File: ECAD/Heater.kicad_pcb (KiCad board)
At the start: 2 copper layers, 200 x 200 mm, 11 parts, among them J1 Conn_01x01_Female, J2 Conn_01x01_Female

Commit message: Cleanup
Renamed files, removed temp files
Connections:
- net /+ renamed Net-(J1-Pad1)
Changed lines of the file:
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@@
-(kicad_pcb (version 20171130) (host pcbnew "(5.1.9)-1")
+(kicad_pcb (version 20171130) (host pcbnew "(5.1.10)-1")
   (general
     (thickness 1.6)
@@
   )
   (net 0 "")
-  (net 1 /+)
+  (net 1 "Net-(J1-Pad1)")
   (net_class Default "This is the default net class."
     (clearance 0.2)
@@
     (uvia_dia 0.3)
     (uvia_drill 0.1)
-    (add_net /+)
+    (add_net "Net-(J1-Pad1)")
   )
   (module MountingHole:MountingHole_3.2mm_M3 (layer F.Cu)
@@
       (effects (font (size 1 1) (thickness 0.15)))
     )
-    (fp_circle (center 0 0) (end 3.45 0) (layer F.CrtYd) (width 0.05))
-    (fp_circle (center 0 0) (end 3.2 0) (layer Cmts.User) (width 0.15))
+    (fp_circle (center 0 0) (end 3.2 0) (layer Cmts.User) (width 0.15))
+    (fp_circle (center 0 0) (end 3.45 0) (layer F.CrtYd) (width 0.05))
     (fp_text user %R (at 0.3 0) (layer F.Fab)
       (effects (font (size 1 1) (thickness 0.15)))
@@
       (effects (font (size 1 1) (thickness 0.15)))
     )
-    (fp_circle (center 0 0) (end 3.45 0) (layer F.CrtYd) (width 0.05))
-    (fp_circle (center 0 0) (end 3.2 0) (layer Cmts.User) (width 0.15))
+    (fp_circle (center 0 0) (end 3.2 0) (layer Cmts.User) (width 0.15))
+    (fp_circle (center 0 0) (end 3.45 0) (layer F.CrtYd) (width 0.05))
     (fp_text user %R (at 0.3 0) (layer F.Fab)
       (effects (font (size 1 1) (thickness 0.15)))
@@
       (effects (font (size 1 1) (thickness 0.15)))
     )
-    (fp_circle (center 0 0) (end 3.45 0) (layer F.CrtYd) (width 0.05))
-    (fp_circle (center 0 0) (end 3.2 0) (layer Cmts.User) (width 0.15))
+    (fp_circle (center 0 0) (end 3.2 0) (layer Cmts.User) (width 0.15))
+    (fp_circle (center 0 0) (end 3.45 0) (layer F.CrtYd) (width 0.05))
     (fp_text user %R (at 0.3 0) (layer F.Fab)
       (effects (font (size 1 1) (thickness 0.15)))
@@
       (effects (font (size 1 1) (thickness 0.15)))
     )
-    (fp_circle (center 0 0) (end 3.45 0) (layer F.CrtYd) (width 0.05))
-    (fp_circle (center 0 0) (end 3.2 0) (layer Cmts.User) (width 0.15))
+    (fp_circle (center 0 0) (end 3.2 0) (layer Cmts.User) (width 0.15))
+    (fp_circle (center 0 0) (end 3.45 0) (layer F.CrtYd) (width 0.05))
     (fp_text user %R (at 0.3 0) (layer F.Fab)
       (effects (font (size 1 1) (thickness 0.15)))
@@
       (effects (font (size 1 1) (thickness 0.15)))
     )
-    (fp_circle (center 0 0) (end 3.45 0) (layer F.CrtYd) (width 0.05))
-    (fp_circle (center 0 0) (end 3.2 0) (layer Cmts.User) (width 0.15))
+    (fp_circle (center 0 0) (end 3.2 0) (layer Cmts.User) (width 0.15))
+    (fp_circle (center 0 0) (end 3.45 0) (layer F.CrtYd) (width 0.05))
     (fp_text user %R (at 0.3 0) (layer F.Fab)
       (effects (font (size 1 1) (thickness 0.15)))
@@
       (effects (font (size 1 1) (thickness 0.15)))
     )
-    (fp_circle (center 0 0) (end 3.45 0) (layer F.CrtYd) (width 0.05))
-    (fp_circle (center 0 0) (end 3.2 0) (layer Cmts.User) (width 0.15))
+    (fp_circle (center 0 0) (end 3.2 0) (layer Cmts.User) (width 0.15))
+    (fp_circle (center 0 0) (end 3.45 0) (layer F.CrtYd) (width 0.05))
     (fp_text user %R (at 0.3 0) (layer F.Fab)
       (effects (font (size 1 1) (thickness 0.15)))
@@
       (effects (font (size 1 1) (thickness 0.15)))
     )
-    (fp_circle (center 0 0) (end 3.45 0) (layer F.CrtYd) (width 0.05))
-    (fp_circle (center 0 0) (end 3.2 0) (layer Cmts.User) (width 0.15))
+    (fp_circle (center 0 0) (end 3.2 0) (layer Cmts.User) (width 0.15))
+    (fp_circle (center 0 0) (end 3.45 0) (layer F.CrtYd) (width 0.05))
     (fp_text user %R (at 0.3 0) (layer F.Fab)
       (effects (font (size 1 1) (thickness 0.15)))
@@
       (effects (font (size 1 1) (thickness 0.15)))
     )
-    (fp_circle (center 0 0) (end 3.45 0) (layer F.CrtYd) (width 0.05))
-    (fp_circle (center 0 0) (end 3.2 0) (layer Cmts.User) (width 0.15))
+    (fp_circle (center 0 0) (end 3.2 0) (layer Cmts.User) (width 0.15))
+    (fp_circle (center 0 0) (end 3.45 0) (layer F.CrtYd) (width 0.05))
     (fp_text user %R (at 0.3 0) (layer F.Fab)
       (effects (font (size 1 1) (thickness 0.15)))
@@
       (effects (font (size 1 1) (thickness 0.15)))
     )
-    (fp_circle (center 0 0) (end 3.45 0) (layer F.CrtYd) (width 0.05))
-    (fp_circle (center 0 0) (end 3.2 0) (layer Cmts.User) (width 0.15))
+    (fp_circle (center 0 0) (end 3.2 0) (layer Cmts.User) (width 0.15))
+    (fp_circle (center 0 0) (end 3.45 0) (layer F.CrtYd) (width 0.05))
     (fp_text user %R (at 0.3 0) (layer F.Fab)
       (effects (font (size 1 1) (thickness 0.15)))
@@
     )
     (pad 1 thru_hole rect (at 0 0) (size 6 6) (drill 3.2) (layers *.Cu *.Mask)
-      (net 1 /+))
+      (net 1 "Net-(J1-Pad1)"))
   )
   (module Connectors:M3-Pad (layer F.Cu)
@@
     )
     (pad 1 thru_hole rect (at 0 0) (size 6 6) (drill 3.2) (layers *.Cu *.Mask)
-      (net 1 /+))
+      (net 1 "Net-(J1-Pad1)"))
   )
   (gr_arc (start 85.725 26.035) (end 85.725 30.48) (angle -180) (layer Edge.Cuts) (width 0.05))

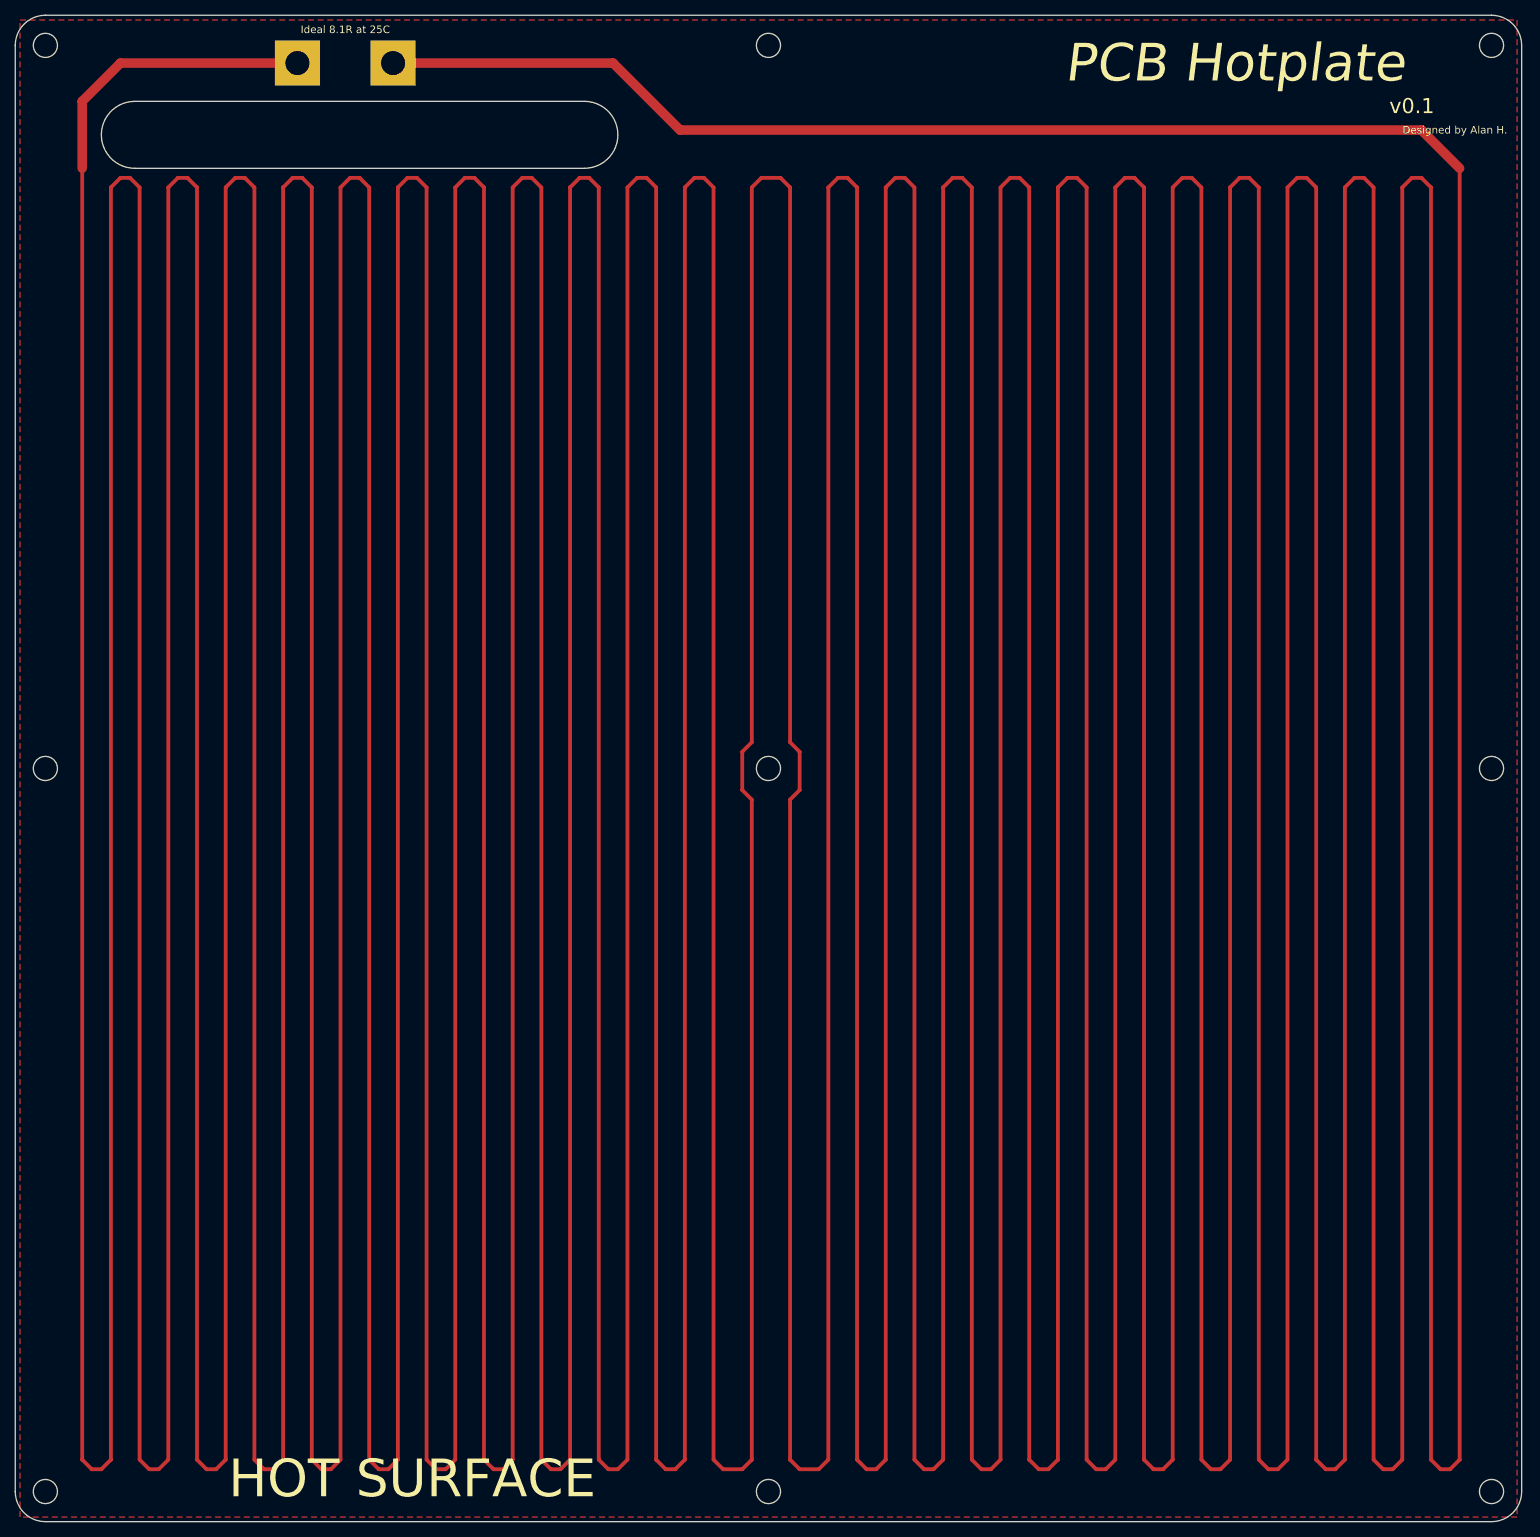
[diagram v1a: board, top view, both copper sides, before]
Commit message: Perforate Heatbed
Added a grid of 2.1mm holes, which may help thermal performance.
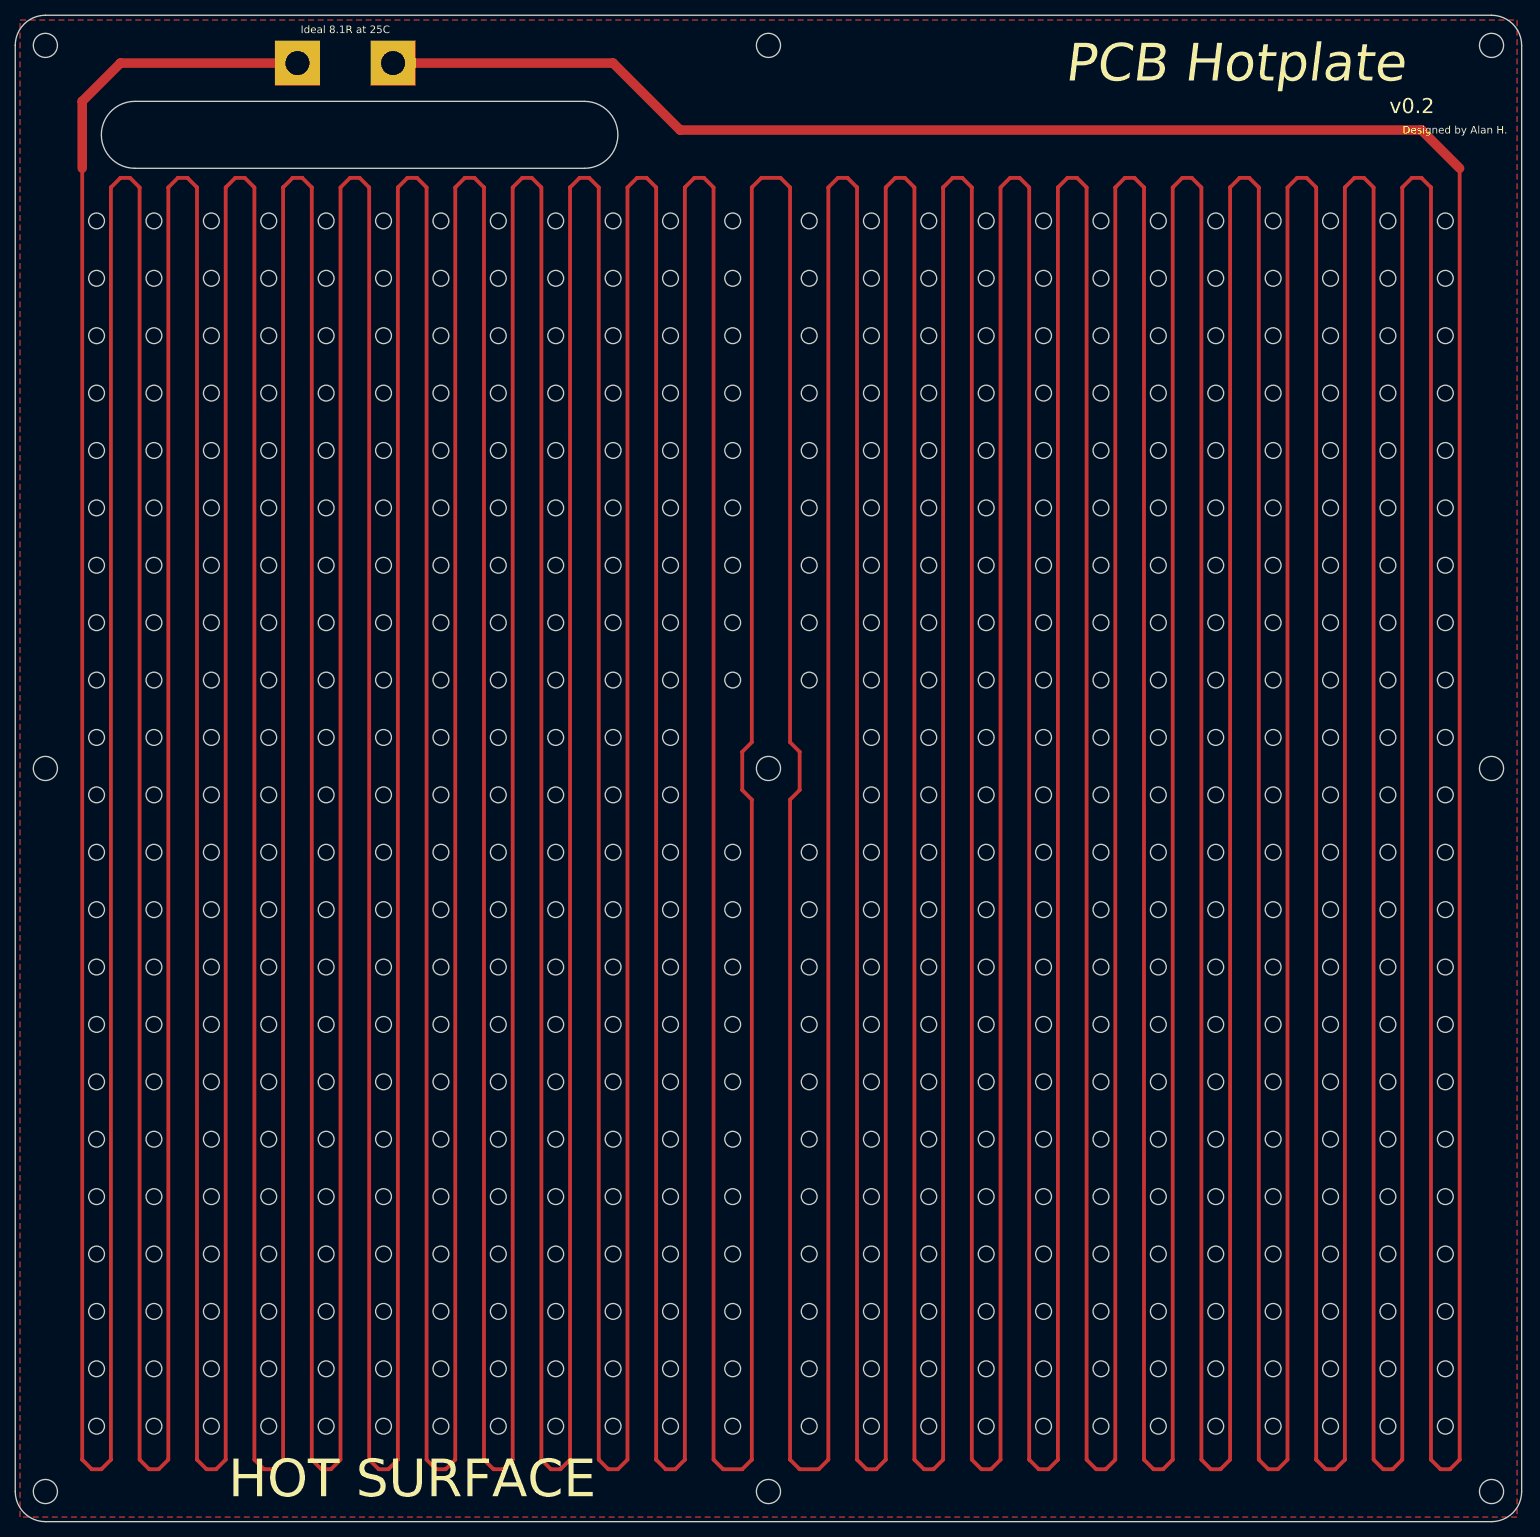
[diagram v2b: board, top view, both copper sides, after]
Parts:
- added REF**: MountingHole_2.1mm, MountingHole:MountingHole_2.1mm, F.Cu at (97.2, 37.5)
- added REF**: MountingHole_2.1mm, MountingHole:MountingHole_2.1mm, F.Cu at (81.9, 37.5)
- added REF**: MountingHole_2.1mm, MountingHole:MountingHole_2.1mm, F.Cu at (146.7, 67.9)
- added REF**: MountingHole_2.1mm, MountingHole:MountingHole_2.1mm, F.Cu at (89.5, 67.9)
- added REF**: MountingHole_2.1mm, MountingHole:MountingHole_2.1mm, F.Cu at (139.1, 67.9)
- added REF**: MountingHole_2.1mm, MountingHole:MountingHole_2.1mm, F.Cu at (123.8, 67.9)
- added REF**: MountingHole_2.1mm, MountingHole:MountingHole_2.1mm, F.Cu at (105.4, 67.9)
- added REF**: MountingHole_2.1mm, MountingHole:MountingHole_2.1mm, F.Cu at (115.6, 67.9)
- added REF**: MountingHole_2.1mm, MountingHole:MountingHole_2.1mm, F.Cu at (81.9, 67.9)
- added REF**: MountingHole_2.1mm, MountingHole:MountingHole_2.1mm, F.Cu at (74.3, 67.9)
- added REF**: MountingHole_2.1mm, MountingHole:MountingHole_2.1mm, F.Cu at (66.7, 67.9)
- added REF**: MountingHole_2.1mm, MountingHole:MountingHole_2.1mm, F.Cu at (51.4, 67.9)
- added REF**: MountingHole_2.1mm, MountingHole:MountingHole_2.1mm, F.Cu at (74.3, 37.5)
- added REF**: MountingHole_2.1mm, MountingHole:MountingHole_2.1mm, F.Cu at (59.1, 67.9)
- added REF**: MountingHole_2.1mm, MountingHole:MountingHole_2.1mm, F.Cu at (43.8, 67.9)
- added REF**: MountingHole_2.1mm, MountingHole:MountingHole_2.1mm, F.Cu at (28.6, 67.9)
- added REF**: MountingHole_2.1mm, MountingHole:MountingHole_2.1mm, F.Cu at (21.0, 67.9)
- added REF**: MountingHole_2.1mm, MountingHole:MountingHole_2.1mm, F.Cu at (200.0, 75.6)
- added REF**: MountingHole_2.1mm, MountingHole:MountingHole_2.1mm, F.Cu at (192.4, 75.6)
- added REF**: MountingHole_2.1mm, MountingHole:MountingHole_2.1mm, F.Cu at (184.8, 75.6)
- added REF**: MountingHole_2.1mm, MountingHole:MountingHole_2.1mm, F.Cu at (177.2, 75.6)
- added REF**: MountingHole_2.1mm, MountingHole:MountingHole_2.1mm, F.Cu at (169.5, 75.6)
- added REF**: MountingHole_2.1mm, MountingHole:MountingHole_2.1mm, F.Cu at (146.7, 75.6)
- added REF**: MountingHole_2.1mm, MountingHole:MountingHole_2.1mm, F.Cu at (66.7, 37.5)
- added REF**: MountingHole_2.1mm, MountingHole:MountingHole_2.1mm, F.Cu at (161.9, 75.6)
- added REF**: MountingHole_2.1mm, MountingHole:MountingHole_2.1mm, F.Cu at (154.3, 75.6)
- added REF**: MountingHole_2.1mm, MountingHole:MountingHole_2.1mm, F.Cu at (139.1, 75.6)
- added REF**: MountingHole_2.1mm, MountingHole:MountingHole_2.1mm, F.Cu at (131.4, 75.6)
- added REF**: MountingHole_2.1mm, MountingHole:MountingHole_2.1mm, F.Cu at (123.8, 75.6)
- added REF**: MountingHole_2.1mm, MountingHole:MountingHole_2.1mm, F.Cu at (115.6, 75.6)
- added REF**: MountingHole_2.1mm, MountingHole:MountingHole_2.1mm, F.Cu at (105.4, 75.6)
- added REF**: MountingHole_2.1mm, MountingHole:MountingHole_2.1mm, F.Cu at (97.2, 75.6)
- added REF**: MountingHole_2.1mm, MountingHole:MountingHole_2.1mm, F.Cu at (89.5, 75.6)
- added REF**: MountingHole_2.1mm, MountingHole:MountingHole_2.1mm, F.Cu at (51.4, 75.6)
- added REF**: MountingHole_2.1mm, MountingHole:MountingHole_2.1mm, F.Cu at (51.4, 37.5)
- added REF**: MountingHole_2.1mm, MountingHole:MountingHole_2.1mm, F.Cu at (43.8, 75.6)
- added REF**: MountingHole_2.1mm, MountingHole:MountingHole_2.1mm, F.Cu at (36.2, 75.6)
- added REF**: MountingHole_2.1mm, MountingHole:MountingHole_2.1mm, F.Cu at (36.2, 67.9)
- added REF**: MountingHole_2.1mm, MountingHole:MountingHole_2.1mm, F.Cu at (66.7, 75.6)
- added REF**: MountingHole_2.1mm, MountingHole:MountingHole_2.1mm, F.Cu at (81.9, 75.6)
- added REF**: MountingHole_2.1mm, MountingHole:MountingHole_2.1mm, F.Cu at (59.1, 75.6)
- added REF**: MountingHole_2.1mm, MountingHole:MountingHole_2.1mm, F.Cu at (74.3, 75.6)
- added REF**: MountingHole_2.1mm, MountingHole:MountingHole_2.1mm, F.Cu at (28.6, 75.6)
- added REF**: MountingHole_2.1mm, MountingHole:MountingHole_2.1mm, F.Cu at (21.0, 75.6)
- added REF**: MountingHole_2.1mm, MountingHole:MountingHole_2.1mm, F.Cu at (192.4, 67.9)
- added REF**: MountingHole_2.1mm, MountingHole:MountingHole_2.1mm, F.Cu at (59.1, 37.5)
- added REF**: MountingHole_2.1mm, MountingHole:MountingHole_2.1mm, F.Cu at (161.9, 67.9)
- added REF**: MountingHole_2.1mm, MountingHole:MountingHole_2.1mm, F.Cu at (169.5, 67.9)
- added REF**: MountingHole_2.1mm, MountingHole:MountingHole_2.1mm, F.Cu at (184.8, 67.9)
- added REF**: MountingHole_2.1mm, MountingHole:MountingHole_2.1mm, F.Cu at (200.0, 67.9)
- added REF**: MountingHole_2.1mm, MountingHole:MountingHole_2.1mm, F.Cu at (177.2, 67.9)
- added REF**: MountingHole_2.1mm, MountingHole:MountingHole_2.1mm, F.Cu at (97.2, 83.2)
- added REF**: MountingHole_2.1mm, MountingHole:MountingHole_2.1mm, F.Cu at (131.4, 83.2)
- added REF**: MountingHole_2.1mm, MountingHole:MountingHole_2.1mm, F.Cu at (154.3, 83.2)
- added REF**: MountingHole_2.1mm, MountingHole:MountingHole_2.1mm, F.Cu at (146.7, 83.2)
- added REF**: MountingHole_2.1mm, MountingHole:MountingHole_2.1mm, F.Cu at (89.5, 83.2)
- added REF**: MountingHole_2.1mm, MountingHole:MountingHole_2.1mm, F.Cu at (43.8, 37.5)
- added REF**: MountingHole_2.1mm, MountingHole:MountingHole_2.1mm, F.Cu at (139.1, 83.2)
- added REF**: MountingHole_2.1mm, MountingHole:MountingHole_2.1mm, F.Cu at (123.8, 83.2)
- added REF**: MountingHole_2.1mm, MountingHole:MountingHole_2.1mm, F.Cu at (105.4, 83.2)
- added REF**: MountingHole_2.1mm, MountingHole:MountingHole_2.1mm, F.Cu at (115.6, 83.2)
- added REF**: MountingHole_2.1mm, MountingHole:MountingHole_2.1mm, F.Cu at (81.9, 83.2)
- added REF**: MountingHole_2.1mm, MountingHole:MountingHole_2.1mm, F.Cu at (74.3, 83.2)
- added REF**: MountingHole_2.1mm, MountingHole:MountingHole_2.1mm, F.Cu at (66.7, 83.2)
- added REF**: MountingHole_2.1mm, MountingHole:MountingHole_2.1mm, F.Cu at (51.4, 83.2)
- added REF**: MountingHole_2.1mm, MountingHole:MountingHole_2.1mm, F.Cu at (59.1, 83.2)
- added REF**: MountingHole_2.1mm, MountingHole:MountingHole_2.1mm, F.Cu at (43.8, 83.2)
- added REF**: MountingHole_2.1mm, MountingHole:MountingHole_2.1mm, F.Cu at (28.6, 37.5)
- added REF**: MountingHole_2.1mm, MountingHole:MountingHole_2.1mm, F.Cu at (28.6, 83.2)
- added REF**: MountingHole_2.1mm, MountingHole:MountingHole_2.1mm, F.Cu at (21.0, 83.2)
- added REF**: MountingHole_2.1mm, MountingHole:MountingHole_2.1mm, F.Cu at (200.0, 90.8)
- added REF**: MountingHole_2.1mm, MountingHole:MountingHole_2.1mm, F.Cu at (192.4, 90.8)
- added REF**: MountingHole_2.1mm, MountingHole:MountingHole_2.1mm, F.Cu at (184.8, 90.8)
- added REF**: MountingHole_2.1mm, MountingHole:MountingHole_2.1mm, F.Cu at (177.2, 90.8)
- added REF**: MountingHole_2.1mm, MountingHole:MountingHole_2.1mm, F.Cu at (169.5, 90.8)
- added REF**: MountingHole_2.1mm, MountingHole:MountingHole_2.1mm, F.Cu at (146.7, 90.8)
- added REF**: MountingHole_2.1mm, MountingHole:MountingHole_2.1mm, F.Cu at (161.9, 90.8)
- added REF**: MountingHole_2.1mm, MountingHole:MountingHole_2.1mm, F.Cu at (154.3, 90.8)
- added REF**: MountingHole_2.1mm, MountingHole:MountingHole_2.1mm, F.Cu at (21.0, 37.5)
- added REF**: MountingHole_2.1mm, MountingHole:MountingHole_2.1mm, F.Cu at (139.1, 90.8)
- added REF**: MountingHole_2.1mm, MountingHole:MountingHole_2.1mm, F.Cu at (131.4, 90.8)
- added REF**: MountingHole_2.1mm, MountingHole:MountingHole_2.1mm, F.Cu at (123.8, 90.8)
- added REF**: MountingHole_2.1mm, MountingHole:MountingHole_2.1mm, F.Cu at (115.6, 90.8)
- added REF**: MountingHole_2.1mm, MountingHole:MountingHole_2.1mm, F.Cu at (105.4, 90.8)
- added REF**: MountingHole_2.1mm, MountingHole:MountingHole_2.1mm, F.Cu at (97.2, 90.8)
- added REF**: MountingHole_2.1mm, MountingHole:MountingHole_2.1mm, F.Cu at (89.5, 90.8)
- added REF**: MountingHole_2.1mm, MountingHole:MountingHole_2.1mm, F.Cu at (51.4, 90.8)
- added REF**: MountingHole_2.1mm, MountingHole:MountingHole_2.1mm, F.Cu at (43.8, 90.8)
- added REF**: MountingHole_2.1mm, MountingHole:MountingHole_2.1mm, F.Cu at (36.2, 90.8)
- added REF**: MountingHole_2.1mm, MountingHole:MountingHole_2.1mm, F.Cu at (200.0, 45.1)
- added REF**: MountingHole_2.1mm, MountingHole:MountingHole_2.1mm, F.Cu at (36.2, 83.2)
- added REF**: MountingHole_2.1mm, MountingHole:MountingHole_2.1mm, F.Cu at (66.7, 90.8)
- added REF**: MountingHole_2.1mm, MountingHole:MountingHole_2.1mm, F.Cu at (81.9, 90.8)
- added REF**: MountingHole_2.1mm, MountingHole:MountingHole_2.1mm, F.Cu at (59.1, 90.8)
- added REF**: MountingHole_2.1mm, MountingHole:MountingHole_2.1mm, F.Cu at (74.3, 90.8)
- added REF**: MountingHole_2.1mm, MountingHole:MountingHole_2.1mm, F.Cu at (28.6, 90.8)
- added REF**: MountingHole_2.1mm, MountingHole:MountingHole_2.1mm, F.Cu at (21.0, 90.8)
- added REF**: MountingHole_2.1mm, MountingHole:MountingHole_2.1mm, F.Cu at (192.4, 83.2)
- added REF**: MountingHole_2.1mm, MountingHole:MountingHole_2.1mm, F.Cu at (161.9, 83.2)
- added REF**: MountingHole_2.1mm, MountingHole:MountingHole_2.1mm, F.Cu at (169.5, 83.2)
- added REF**: MountingHole_2.1mm, MountingHole:MountingHole_2.1mm, F.Cu at (192.4, 45.1)
- added REF**: MountingHole_2.1mm, MountingHole:MountingHole_2.1mm, F.Cu at (184.8, 83.2)
- added REF**: MountingHole_2.1mm, MountingHole:MountingHole_2.1mm, F.Cu at (200.0, 83.2)
- added REF**: MountingHole_2.1mm, MountingHole:MountingHole_2.1mm, F.Cu at (177.2, 83.2)
- added REF**: MountingHole_2.1mm, MountingHole:MountingHole_2.1mm, F.Cu at (97.2, 98.4)
- added REF**: MountingHole_2.1mm, MountingHole:MountingHole_2.1mm, F.Cu at (131.4, 98.4)
- added REF**: MountingHole_2.1mm, MountingHole:MountingHole_2.1mm, F.Cu at (154.3, 98.4)
- added REF**: MountingHole_2.1mm, MountingHole:MountingHole_2.1mm, F.Cu at (146.7, 98.4)
- added REF**: MountingHole_2.1mm, MountingHole:MountingHole_2.1mm, F.Cu at (89.5, 98.4)
- added REF**: MountingHole_2.1mm, MountingHole:MountingHole_2.1mm, F.Cu at (139.1, 98.4)
- added REF**: MountingHole_2.1mm, MountingHole:MountingHole_2.1mm, F.Cu at (123.8, 98.4)
- added REF**: MountingHole_2.1mm, MountingHole:MountingHole_2.1mm, F.Cu at (131.4, 37.5)
- added REF**: MountingHole_2.1mm, MountingHole:MountingHole_2.1mm, F.Cu at (184.8, 45.1)
- added REF**: MountingHole_2.1mm, MountingHole:MountingHole_2.1mm, F.Cu at (105.4, 98.4)
- added REF**: MountingHole_2.1mm, MountingHole:MountingHole_2.1mm, F.Cu at (115.6, 98.4)
- added REF**: MountingHole_2.1mm, MountingHole:MountingHole_2.1mm, F.Cu at (81.9, 98.4)
- added REF**: MountingHole_2.1mm, MountingHole:MountingHole_2.1mm, F.Cu at (74.3, 98.4)
- added REF**: MountingHole_2.1mm, MountingHole:MountingHole_2.1mm, F.Cu at (66.7, 98.4)
- added REF**: MountingHole_2.1mm, MountingHole:MountingHole_2.1mm, F.Cu at (51.4, 98.4)
- added REF**: MountingHole_2.1mm, MountingHole:MountingHole_2.1mm, F.Cu at (59.1, 98.4)
- added REF**: MountingHole_2.1mm, MountingHole:MountingHole_2.1mm, F.Cu at (43.8, 98.4)
- added REF**: MountingHole_2.1mm, MountingHole:MountingHole_2.1mm, F.Cu at (28.6, 98.4)
- added REF**: MountingHole_2.1mm, MountingHole:MountingHole_2.1mm, F.Cu at (21.0, 98.4)
- added REF**: MountingHole_2.1mm, MountingHole:MountingHole_2.1mm, F.Cu at (177.2, 45.1)
- added REF**: MountingHole_2.1mm, MountingHole:MountingHole_2.1mm, F.Cu at (200.0, 106.0)
- added REF**: MountingHole_2.1mm, MountingHole:MountingHole_2.1mm, F.Cu at (192.4, 106.0)
- added REF**: MountingHole_2.1mm, MountingHole:MountingHole_2.1mm, F.Cu at (184.8, 106.0)
- added REF**: MountingHole_2.1mm, MountingHole:MountingHole_2.1mm, F.Cu at (177.2, 106.0)
- added REF**: MountingHole_2.1mm, MountingHole:MountingHole_2.1mm, F.Cu at (169.5, 106.0)
- added REF**: MountingHole_2.1mm, MountingHole:MountingHole_2.1mm, F.Cu at (146.7, 106.0)
- added REF**: MountingHole_2.1mm, MountingHole:MountingHole_2.1mm, F.Cu at (161.9, 106.0)
- added REF**: MountingHole_2.1mm, MountingHole:MountingHole_2.1mm, F.Cu at (154.3, 106.0)
- added REF**: MountingHole_2.1mm, MountingHole:MountingHole_2.1mm, F.Cu at (139.1, 106.0)
- added REF**: MountingHole_2.1mm, MountingHole:MountingHole_2.1mm, F.Cu at (131.4, 106.0)
- added REF**: MountingHole_2.1mm, MountingHole:MountingHole_2.1mm, F.Cu at (169.5, 45.1)
- added REF**: MountingHole_2.1mm, MountingHole:MountingHole_2.1mm, F.Cu at (123.8, 106.0)
- added REF**: MountingHole_2.1mm, MountingHole:MountingHole_2.1mm, F.Cu at (97.2, 106.0)
- added REF**: MountingHole_2.1mm, MountingHole:MountingHole_2.1mm, F.Cu at (89.5, 106.0)
- added REF**: MountingHole_2.1mm, MountingHole:MountingHole_2.1mm, F.Cu at (51.4, 106.0)
- added REF**: MountingHole_2.1mm, MountingHole:MountingHole_2.1mm, F.Cu at (43.8, 106.0)
- added REF**: MountingHole_2.1mm, MountingHole:MountingHole_2.1mm, F.Cu at (36.2, 106.0)
- added REF**: MountingHole_2.1mm, MountingHole:MountingHole_2.1mm, F.Cu at (36.2, 98.4)
- added REF**: MountingHole_2.1mm, MountingHole:MountingHole_2.1mm, F.Cu at (66.7, 106.0)
- added REF**: MountingHole_2.1mm, MountingHole:MountingHole_2.1mm, F.Cu at (81.9, 106.0)
- added REF**: MountingHole_2.1mm, MountingHole:MountingHole_2.1mm, F.Cu at (59.1, 106.0)
- added REF**: MountingHole_2.1mm, MountingHole:MountingHole_2.1mm, F.Cu at (146.7, 45.1)
- added REF**: MountingHole_2.1mm, MountingHole:MountingHole_2.1mm, F.Cu at (74.3, 106.0)
- added REF**: MountingHole_2.1mm, MountingHole:MountingHole_2.1mm, F.Cu at (28.6, 106.0)
- added REF**: MountingHole_2.1mm, MountingHole:MountingHole_2.1mm, F.Cu at (21.0, 106.0)
- added REF**: MountingHole_2.1mm, MountingHole:MountingHole_2.1mm, F.Cu at (192.4, 98.4)
- added REF**: MountingHole_2.1mm, MountingHole:MountingHole_2.1mm, F.Cu at (161.9, 98.4)
- added REF**: MountingHole_2.1mm, MountingHole:MountingHole_2.1mm, F.Cu at (169.5, 98.4)
- added REF**: MountingHole_2.1mm, MountingHole:MountingHole_2.1mm, F.Cu at (184.8, 98.4)
- added REF**: MountingHole_2.1mm, MountingHole:MountingHole_2.1mm, F.Cu at (200.0, 98.4)
- added REF**: MountingHole_2.1mm, MountingHole:MountingHole_2.1mm, F.Cu at (177.2, 98.4)
- added REF**: MountingHole_2.1mm, MountingHole:MountingHole_2.1mm, F.Cu at (97.2, 113.7)
- added REF**: MountingHole_2.1mm, MountingHole:MountingHole_2.1mm, F.Cu at (161.9, 45.1)
- added REF**: MountingHole_2.1mm, MountingHole:MountingHole_2.1mm, F.Cu at (131.4, 113.7)
- added REF**: MountingHole_2.1mm, MountingHole:MountingHole_2.1mm, F.Cu at (154.3, 113.7)
- added REF**: MountingHole_2.1mm, MountingHole:MountingHole_2.1mm, F.Cu at (146.7, 113.7)
- added REF**: MountingHole_2.1mm, MountingHole:MountingHole_2.1mm, F.Cu at (89.5, 113.7)
- added REF**: MountingHole_2.1mm, MountingHole:MountingHole_2.1mm, F.Cu at (139.1, 113.7)
- added REF**: MountingHole_2.1mm, MountingHole:MountingHole_2.1mm, F.Cu at (123.8, 113.7)
- added REF**: MountingHole_2.1mm, MountingHole:MountingHole_2.1mm, F.Cu at (81.9, 113.7)
- added REF**: MountingHole_2.1mm, MountingHole:MountingHole_2.1mm, F.Cu at (74.3, 113.7)
- added REF**: MountingHole_2.1mm, MountingHole:MountingHole_2.1mm, F.Cu at (66.7, 113.7)
- added REF**: MountingHole_2.1mm, MountingHole:MountingHole_2.1mm, F.Cu at (51.4, 113.7)
- added REF**: MountingHole_2.1mm, MountingHole:MountingHole_2.1mm, F.Cu at (154.3, 45.1)
- added REF**: MountingHole_2.1mm, MountingHole:MountingHole_2.1mm, F.Cu at (59.1, 113.7)
- added REF**: MountingHole_2.1mm, MountingHole:MountingHole_2.1mm, F.Cu at (43.8, 113.7)
- added REF**: MountingHole_2.1mm, MountingHole:MountingHole_2.1mm, F.Cu at (28.6, 113.7)
- added REF**: MountingHole_2.1mm, MountingHole:MountingHole_2.1mm, F.Cu at (21.0, 113.7)
- added REF**: MountingHole_2.1mm, MountingHole:MountingHole_2.1mm, F.Cu at (200.0, 121.3)
- added REF**: MountingHole_2.1mm, MountingHole:MountingHole_2.1mm, F.Cu at (192.4, 121.3)
- added REF**: MountingHole_2.1mm, MountingHole:MountingHole_2.1mm, F.Cu at (184.8, 121.3)
- added REF**: MountingHole_2.1mm, MountingHole:MountingHole_2.1mm, F.Cu at (177.2, 121.3)
- added REF**: MountingHole_2.1mm, MountingHole:MountingHole_2.1mm, F.Cu at (169.5, 121.3)
- added REF**: MountingHole_2.1mm, MountingHole:MountingHole_2.1mm, F.Cu at (146.7, 121.3)
- added REF**: MountingHole_2.1mm, MountingHole:MountingHole_2.1mm, F.Cu at (139.1, 45.1)
- added REF**: MountingHole_2.1mm, MountingHole:MountingHole_2.1mm, F.Cu at (161.9, 121.3)
- added REF**: MountingHole_2.1mm, MountingHole:MountingHole_2.1mm, F.Cu at (154.3, 121.3)
- added REF**: MountingHole_2.1mm, MountingHole:MountingHole_2.1mm, F.Cu at (139.1, 121.3)
- added REF**: MountingHole_2.1mm, MountingHole:MountingHole_2.1mm, F.Cu at (131.4, 121.3)
- added REF**: MountingHole_2.1mm, MountingHole:MountingHole_2.1mm, F.Cu at (123.8, 121.3)
- added REF**: MountingHole_2.1mm, MountingHole:MountingHole_2.1mm, F.Cu at (115.6, 121.3)
- added REF**: MountingHole_2.1mm, MountingHole:MountingHole_2.1mm, F.Cu at (105.4, 121.3)
- added REF**: MountingHole_2.1mm, MountingHole:MountingHole_2.1mm, F.Cu at (97.2, 121.3)
- added REF**: MountingHole_2.1mm, MountingHole:MountingHole_2.1mm, F.Cu at (89.5, 121.3)
- added REF**: MountingHole_2.1mm, MountingHole:MountingHole_2.1mm, F.Cu at (51.4, 121.3)
- added REF**: MountingHole_2.1mm, MountingHole:MountingHole_2.1mm, F.Cu at (131.4, 45.1)
- added REF**: MountingHole_2.1mm, MountingHole:MountingHole_2.1mm, F.Cu at (43.8, 121.3)
- added REF**: MountingHole_2.1mm, MountingHole:MountingHole_2.1mm, F.Cu at (36.2, 121.3)
- added REF**: MountingHole_2.1mm, MountingHole:MountingHole_2.1mm, F.Cu at (36.2, 113.7)
- added REF**: MountingHole_2.1mm, MountingHole:MountingHole_2.1mm, F.Cu at (66.7, 121.3)
- added REF**: MountingHole_2.1mm, MountingHole:MountingHole_2.1mm, F.Cu at (81.9, 121.3)
- added REF**: MountingHole_2.1mm, MountingHole:MountingHole_2.1mm, F.Cu at (59.1, 121.3)
- added REF**: MountingHole_2.1mm, MountingHole:MountingHole_2.1mm, F.Cu at (74.3, 121.3)
- added REF**: MountingHole_2.1mm, MountingHole:MountingHole_2.1mm, F.Cu at (28.6, 121.3)
- added REF**: MountingHole_2.1mm, MountingHole:MountingHole_2.1mm, F.Cu at (21.0, 121.3)
- added REF**: MountingHole_2.1mm, MountingHole:MountingHole_2.1mm, F.Cu at (192.4, 113.7)
- added REF**: MountingHole_2.1mm, MountingHole:MountingHole_2.1mm, F.Cu at (123.8, 45.1)
- added REF**: MountingHole_2.1mm, MountingHole:MountingHole_2.1mm, F.Cu at (161.9, 113.7)
- added REF**: MountingHole_2.1mm, MountingHole:MountingHole_2.1mm, F.Cu at (169.5, 113.7)
- added REF**: MountingHole_2.1mm, MountingHole:MountingHole_2.1mm, F.Cu at (184.8, 113.7)
- added REF**: MountingHole_2.1mm, MountingHole:MountingHole_2.1mm, F.Cu at (200.0, 113.7)
- added REF**: MountingHole_2.1mm, MountingHole:MountingHole_2.1mm, F.Cu at (177.2, 113.7)
- added REF**: MountingHole_2.1mm, MountingHole:MountingHole_2.1mm, F.Cu at (97.2, 128.9)
- added REF**: MountingHole_2.1mm, MountingHole:MountingHole_2.1mm, F.Cu at (131.4, 128.9)
- added REF**: MountingHole_2.1mm, MountingHole:MountingHole_2.1mm, F.Cu at (154.3, 128.9)
- added REF**: MountingHole_2.1mm, MountingHole:MountingHole_2.1mm, F.Cu at (146.7, 128.9)
- added REF**: MountingHole_2.1mm, MountingHole:MountingHole_2.1mm, F.Cu at (89.5, 128.9)
- added REF**: MountingHole_2.1mm, MountingHole:MountingHole_2.1mm, F.Cu at (115.6, 45.1)
- added REF**: MountingHole_2.1mm, MountingHole:MountingHole_2.1mm, F.Cu at (139.1, 128.9)
- added REF**: MountingHole_2.1mm, MountingHole:MountingHole_2.1mm, F.Cu at (123.8, 128.9)
- added REF**: MountingHole_2.1mm, MountingHole:MountingHole_2.1mm, F.Cu at (105.4, 128.9)
- added REF**: MountingHole_2.1mm, MountingHole:MountingHole_2.1mm, F.Cu at (115.6, 128.9)
- added REF**: MountingHole_2.1mm, MountingHole:MountingHole_2.1mm, F.Cu at (81.9, 128.9)
- added REF**: MountingHole_2.1mm, MountingHole:MountingHole_2.1mm, F.Cu at (74.3, 128.9)
- added REF**: MountingHole_2.1mm, MountingHole:MountingHole_2.1mm, F.Cu at (66.7, 128.9)
- added REF**: MountingHole_2.1mm, MountingHole:MountingHole_2.1mm, F.Cu at (51.4, 128.9)
- added REF**: MountingHole_2.1mm, MountingHole:MountingHole_2.1mm, F.Cu at (59.1, 128.9)
- added REF**: MountingHole_2.1mm, MountingHole:MountingHole_2.1mm, F.Cu at (43.8, 128.9)
- added REF**: MountingHole_2.1mm, MountingHole:MountingHole_2.1mm, F.Cu at (154.3, 37.5)
- added REF**: MountingHole_2.1mm, MountingHole:MountingHole_2.1mm, F.Cu at (105.4, 45.1)
- added REF**: MountingHole_2.1mm, MountingHole:MountingHole_2.1mm, F.Cu at (28.6, 128.9)
- added REF**: MountingHole_2.1mm, MountingHole:MountingHole_2.1mm, F.Cu at (21.0, 128.9)
- added REF**: MountingHole_2.1mm, MountingHole:MountingHole_2.1mm, F.Cu at (200.0, 136.5)
- added REF**: MountingHole_2.1mm, MountingHole:MountingHole_2.1mm, F.Cu at (192.4, 136.5)
- added REF**: MountingHole_2.1mm, MountingHole:MountingHole_2.1mm, F.Cu at (184.8, 136.5)
- added REF**: MountingHole_2.1mm, MountingHole:MountingHole_2.1mm, F.Cu at (177.2, 136.5)
- added REF**: MountingHole_2.1mm, MountingHole:MountingHole_2.1mm, F.Cu at (169.5, 136.5)
- added REF**: MountingHole_2.1mm, MountingHole:MountingHole_2.1mm, F.Cu at (146.7, 136.5)
- added REF**: MountingHole_2.1mm, MountingHole:MountingHole_2.1mm, F.Cu at (161.9, 136.5)
- added REF**: MountingHole_2.1mm, MountingHole:MountingHole_2.1mm, F.Cu at (154.3, 136.5)
- added REF**: MountingHole_2.1mm, MountingHole:MountingHole_2.1mm, F.Cu at (97.2, 45.1)
- added REF**: MountingHole_2.1mm, MountingHole:MountingHole_2.1mm, F.Cu at (139.1, 136.5)
- added REF**: MountingHole_2.1mm, MountingHole:MountingHole_2.1mm, F.Cu at (131.4, 136.5)
- added REF**: MountingHole_2.1mm, MountingHole:MountingHole_2.1mm, F.Cu at (123.8, 136.5)
- added REF**: MountingHole_2.1mm, MountingHole:MountingHole_2.1mm, F.Cu at (115.6, 136.5)
- added REF**: MountingHole_2.1mm, MountingHole:MountingHole_2.1mm, F.Cu at (105.4, 136.5)
- added REF**: MountingHole_2.1mm, MountingHole:MountingHole_2.1mm, F.Cu at (97.2, 136.5)
- added REF**: MountingHole_2.1mm, MountingHole:MountingHole_2.1mm, F.Cu at (89.5, 136.5)
- added REF**: MountingHole_2.1mm, MountingHole:MountingHole_2.1mm, F.Cu at (51.4, 136.5)
- added REF**: MountingHole_2.1mm, MountingHole:MountingHole_2.1mm, F.Cu at (43.8, 136.5)
- added REF**: MountingHole_2.1mm, MountingHole:MountingHole_2.1mm, F.Cu at (36.2, 136.5)
- added REF**: MountingHole_2.1mm, MountingHole:MountingHole_2.1mm, F.Cu at (89.5, 45.1)
- added REF**: MountingHole_2.1mm, MountingHole:MountingHole_2.1mm, F.Cu at (36.2, 128.9)
- added REF**: MountingHole_2.1mm, MountingHole:MountingHole_2.1mm, F.Cu at (66.7, 136.5)
- added REF**: MountingHole_2.1mm, MountingHole:MountingHole_2.1mm, F.Cu at (81.9, 136.5)
- added REF**: MountingHole_2.1mm, MountingHole:MountingHole_2.1mm, F.Cu at (59.1, 136.5)
- added REF**: MountingHole_2.1mm, MountingHole:MountingHole_2.1mm, F.Cu at (74.3, 136.5)
- added REF**: MountingHole_2.1mm, MountingHole:MountingHole_2.1mm, F.Cu at (28.6, 136.5)
- added REF**: MountingHole_2.1mm, MountingHole:MountingHole_2.1mm, F.Cu at (21.0, 136.5)
- added REF**: MountingHole_2.1mm, MountingHole:MountingHole_2.1mm, F.Cu at (192.4, 128.9)
- added REF**: MountingHole_2.1mm, MountingHole:MountingHole_2.1mm, F.Cu at (161.9, 128.9)
- added REF**: MountingHole_2.1mm, MountingHole:MountingHole_2.1mm, F.Cu at (169.5, 128.9)
- added REF**: MountingHole_2.1mm, MountingHole:MountingHole_2.1mm, F.Cu at (51.4, 45.1)
- added REF**: MountingHole_2.1mm, MountingHole:MountingHole_2.1mm, F.Cu at (184.8, 128.9)
- added REF**: MountingHole_2.1mm, MountingHole:MountingHole_2.1mm, F.Cu at (200.0, 128.9)
- added REF**: MountingHole_2.1mm, MountingHole:MountingHole_2.1mm, F.Cu at (177.2, 128.9)
- added REF**: MountingHole_2.1mm, MountingHole:MountingHole_2.1mm, F.Cu at (97.2, 144.1)
- added REF**: MountingHole_2.1mm, MountingHole:MountingHole_2.1mm, F.Cu at (131.4, 144.1)
- added REF**: MountingHole_2.1mm, MountingHole:MountingHole_2.1mm, F.Cu at (154.3, 144.1)
- added REF**: MountingHole_2.1mm, MountingHole:MountingHole_2.1mm, F.Cu at (146.7, 144.1)
- added REF**: MountingHole_2.1mm, MountingHole:MountingHole_2.1mm, F.Cu at (89.5, 144.1)
- added REF**: MountingHole_2.1mm, MountingHole:MountingHole_2.1mm, F.Cu at (139.1, 144.1)
- added REF**: MountingHole_2.1mm, MountingHole:MountingHole_2.1mm, F.Cu at (123.8, 144.1)
- added REF**: MountingHole_2.1mm, MountingHole:MountingHole_2.1mm, F.Cu at (43.8, 45.1)
- added REF**: MountingHole_2.1mm, MountingHole:MountingHole_2.1mm, F.Cu at (105.4, 144.1)
- added REF**: MountingHole_2.1mm, MountingHole:MountingHole_2.1mm, F.Cu at (115.6, 144.1)
- added REF**: MountingHole_2.1mm, MountingHole:MountingHole_2.1mm, F.Cu at (81.9, 144.1)
- added REF**: MountingHole_2.1mm, MountingHole:MountingHole_2.1mm, F.Cu at (74.3, 144.1)
- added REF**: MountingHole_2.1mm, MountingHole:MountingHole_2.1mm, F.Cu at (66.7, 144.1)
- added REF**: MountingHole_2.1mm, MountingHole:MountingHole_2.1mm, F.Cu at (51.4, 144.1)
- added REF**: MountingHole_2.1mm, MountingHole:MountingHole_2.1mm, F.Cu at (59.1, 144.1)
- added REF**: MountingHole_2.1mm, MountingHole:MountingHole_2.1mm, F.Cu at (43.8, 144.1)
- added REF**: MountingHole_2.1mm, MountingHole:MountingHole_2.1mm, F.Cu at (28.6, 144.1)
- added REF**: MountingHole_2.1mm, MountingHole:MountingHole_2.1mm, F.Cu at (21.0, 144.1)
- added REF**: MountingHole_2.1mm, MountingHole:MountingHole_2.1mm, F.Cu at (36.2, 45.1)
- added REF**: MountingHole_2.1mm, MountingHole:MountingHole_2.1mm, F.Cu at (200.0, 151.8)
- added REF**: MountingHole_2.1mm, MountingHole:MountingHole_2.1mm, F.Cu at (192.4, 151.8)
- added REF**: MountingHole_2.1mm, MountingHole:MountingHole_2.1mm, F.Cu at (184.8, 151.8)
- added REF**: MountingHole_2.1mm, MountingHole:MountingHole_2.1mm, F.Cu at (177.2, 151.8)
- added REF**: MountingHole_2.1mm, MountingHole:MountingHole_2.1mm, F.Cu at (169.5, 151.8)
- added REF**: MountingHole_2.1mm, MountingHole:MountingHole_2.1mm, F.Cu at (146.7, 151.8)
- added REF**: MountingHole_2.1mm, MountingHole:MountingHole_2.1mm, F.Cu at (161.9, 151.8)
- added REF**: MountingHole_2.1mm, MountingHole:MountingHole_2.1mm, F.Cu at (154.3, 151.8)
- added REF**: MountingHole_2.1mm, MountingHole:MountingHole_2.1mm, F.Cu at (139.1, 151.8)
- added REF**: MountingHole_2.1mm, MountingHole:MountingHole_2.1mm, F.Cu at (131.4, 151.8)
- added REF**: MountingHole_2.1mm, MountingHole:MountingHole_2.1mm, F.Cu at (36.2, 37.5)
- added REF**: MountingHole_2.1mm, MountingHole:MountingHole_2.1mm, F.Cu at (123.8, 151.8)
- added REF**: MountingHole_2.1mm, MountingHole:MountingHole_2.1mm, F.Cu at (115.6, 151.8)
- added REF**: MountingHole_2.1mm, MountingHole:MountingHole_2.1mm, F.Cu at (105.4, 151.8)
- added REF**: MountingHole_2.1mm, MountingHole:MountingHole_2.1mm, F.Cu at (97.2, 151.8)
- added REF**: MountingHole_2.1mm, MountingHole:MountingHole_2.1mm, F.Cu at (89.5, 151.8)
- added REF**: MountingHole_2.1mm, MountingHole:MountingHole_2.1mm, F.Cu at (51.4, 151.8)
- added REF**: MountingHole_2.1mm, MountingHole:MountingHole_2.1mm, F.Cu at (43.8, 151.8)
- added REF**: MountingHole_2.1mm, MountingHole:MountingHole_2.1mm, F.Cu at (36.2, 151.8)
- added REF**: MountingHole_2.1mm, MountingHole:MountingHole_2.1mm, F.Cu at (36.2, 144.1)
- added REF**: MountingHole_2.1mm, MountingHole:MountingHole_2.1mm, F.Cu at (66.7, 151.8)
- added REF**: MountingHole_2.1mm, MountingHole:MountingHole_2.1mm, F.Cu at (66.7, 45.1)
- added REF**: MountingHole_2.1mm, MountingHole:MountingHole_2.1mm, F.Cu at (81.9, 151.8)
- added REF**: MountingHole_2.1mm, MountingHole:MountingHole_2.1mm, F.Cu at (59.1, 151.8)
- added REF**: MountingHole_2.1mm, MountingHole:MountingHole_2.1mm, F.Cu at (74.3, 151.8)
- added REF**: MountingHole_2.1mm, MountingHole:MountingHole_2.1mm, F.Cu at (28.6, 151.8)
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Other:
- board text added: "v0.2"
- board text removed: "v0.1"
